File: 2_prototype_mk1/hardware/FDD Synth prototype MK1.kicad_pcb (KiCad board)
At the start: 2 copper layers, 82 x 57.3 mm, 25 parts, among them J1 Micro_SD_Card, J2 Conn_02x17_Odd_Even, J3 Conn_01x04_Pin, J5 Conn_01x02, J6 Conn_01x04_Pin, U1 74AHCT245, U5 MAX98357A

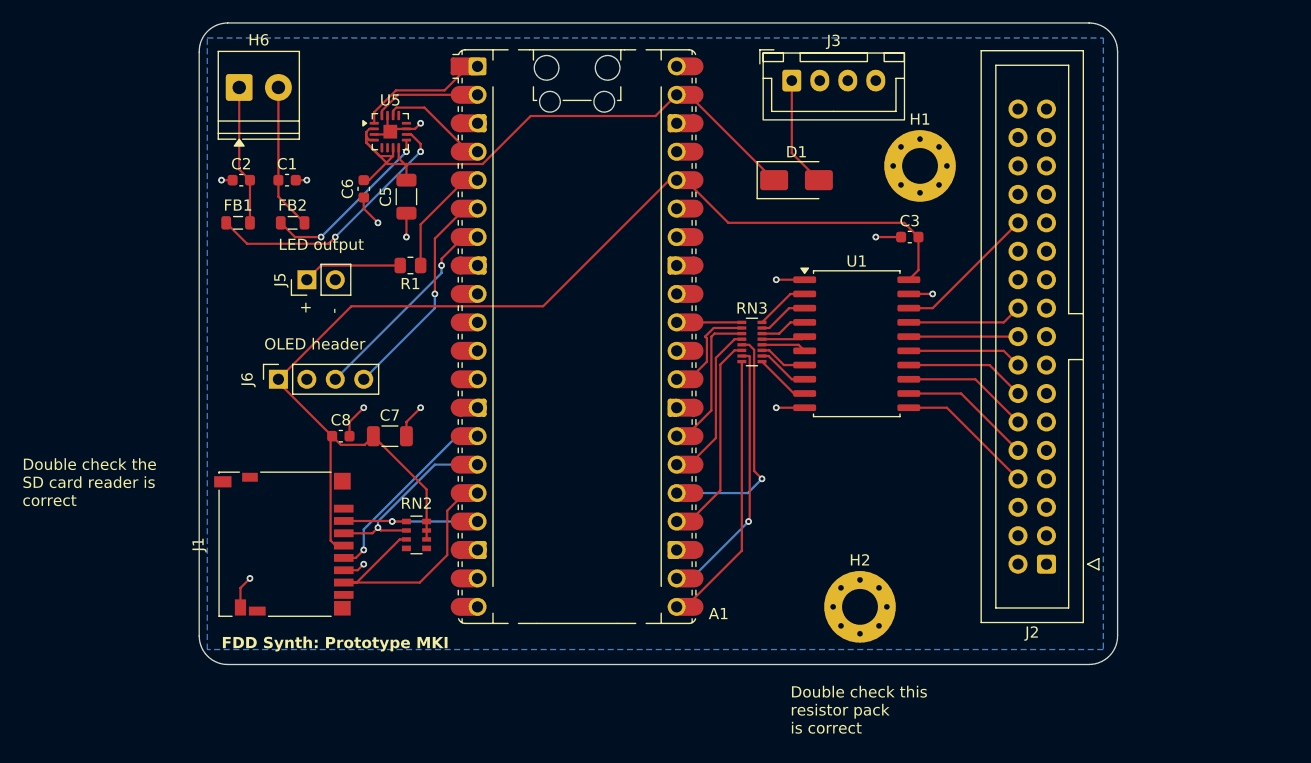
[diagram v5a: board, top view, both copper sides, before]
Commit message: Change power connector and reroute amp
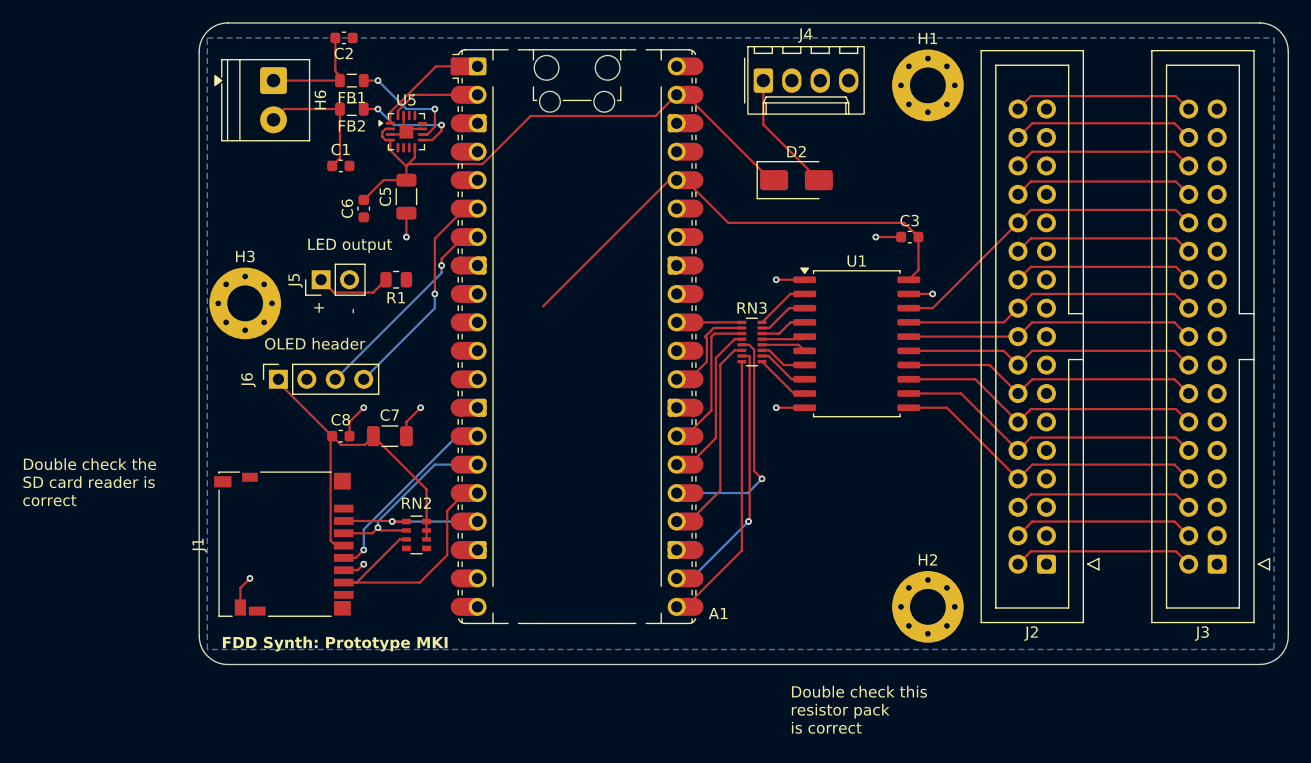
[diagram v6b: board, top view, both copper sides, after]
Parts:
- removed D1: SS14, Diode_SMD:D_SMA
- added D2: SS14, Diode_SMD:D_SMA, F.Cu at (147.9, 83.8)
- added H3: MountingHole_Pad, MountingHole:MountingHole_3.2mm_M3_Pad_Via, F.Cu at (98.6, 94.8)
- added J4: Conn_01x04_Pin, Connector_Molex:Molex_KK-254_AE-6410-04A_1x04_P2.54mm_Vertical, F.Cu at (144.9, 74.9)
- J3: value Conn_01x04_Pin -> Conn_02x17_Odd_Even; footprint Connector_JST:JST_XH_B4B-XH-A_1x04_P2.50mm_Vertical -> Connector_IDC:IDC-Header_2x17_P2.54mm_Vertical
- moved J3 57.5 mm to (185.4, 118.1), turned to 180 degrees
- moved FB1 16.3 mm to (108.2, 74.9), turned to 180 degrees
- moved C2 15.7 mm to (107.5, 71.1), turned to 180 degrees
- moved FB2 11.5 mm to (108.2, 77.5), turned to 180 degrees
- moved H1 7.23 mm to (159.6, 75.4)
- moved H2 6.06 mm to (159.6, 121.9)
- moved C1 4.97 mm to (107.2, 82.5)
- moved H6 3.12 mm to (101.2, 74.9), turned to -90 degrees
- moved R1 1.80 mm to (112.1, 92.7)
- moved C6 1.77 mm to (109.2, 86.4)
- moved U5 1.44 mm to (113.0, 79.5)
- moved J5 1.27 mm to (105.4, 92.7)
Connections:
- J2 pad 2: unconnected-(J2-Pin_2-Pad2) -> Net-(J2-Pin_2)
- J2 pad 22: unconnected-(J2-Pin_22-Pad22) -> Net-(J2-Pin_22)
- J2 pad 24: unconnected-(J2-Pin_24-Pad24) -> Net-(J2-Pin_24)
- J2 pad 28: unconnected-(J2-Pin_28-Pad28) -> Net-(J2-Pin_28)
- J2 pad 30: unconnected-(J2-Pin_30-Pad30) -> Net-(J2-Pin_30)
- J2 pad 32: unconnected-(J2-Pin_32-Pad32) -> Net-(J2-Pin_32)
- J2 pad 34: unconnected-(J2-Pin_34-Pad34) -> Net-(J2-Pin_34)
- J2 pad 4: unconnected-(J2-Pin_4-Pad4) -> Net-(J2-Pin_4)
- J2 pad 6: unconnected-(J2-Pin_6-Pad6) -> Net-(J2-Pin_6)
- J3 pad 1: +5V -> GND
- J3 pad 2: GND -> Net-(J2-Pin_2)
- J3 pad 4: unconnected-(J3-Pin_4-Pad4) -> Net-(J2-Pin_4)
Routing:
- net +3.3V: track 103.3 -> 77.0 mm
- net Net-(J2-Pin_32): track 0.00 -> 16.3 mm
- net /FDD interface/FDD_CONN_DRIVE_SEL_A: track 10.8 -> 27.1 mm
- net /FDD interface/FDD_CONN_DIRECTION: track 9.75 -> 26.0 mm
- net /FDD interface/FDD_CONN_INDEX: track 12.4 -> 28.7 mm
- net Net-(J2-Pin_4): track 0.00 -> 16.3 mm
- net Net-(J2-Pin_30): track 0.00 -> 16.3 mm
- net /FDD interface/FDD_CONN_STEP: track 10.3 -> 26.6 mm
- net /FDD interface/FDD_CONN_MOTOR_EN_B: track 10.3 -> 26.6 mm
- net Net-(J2-Pin_6): track 0.00 -> 16.2 mm
- net Net-(J2-Pin_34): track 0.00 -> 16.2 mm
- net Net-(J2-Pin_28): track 0.00 -> 16.2 mm
- net Net-(J2-Pin_24): track 0.00 -> 16.2 mm
- net Net-(J2-Pin_2): track 0.00 -> 16.2 mm
- net /FDD interface/FDD_CONN_MOTOR_EN_A: track 11.9 -> 28.0 mm
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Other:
- board size 82 x 57.3 mm -> 97.2 x 57.3 mm
